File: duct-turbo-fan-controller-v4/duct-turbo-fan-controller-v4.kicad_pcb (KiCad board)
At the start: 2 copper layers, 42.7 x 48.8 mm, 45 parts, among them J1 Screw_Terminal_01x04, J2 Conn_01x04, J3 USB_OTG, J4 AudioJack4, J7 Conn_01x04, Q1 MMBT3904, Q2 BSS84, SW1 SW_Push, SW2 SW_Push, U1 SCD41-D-R2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

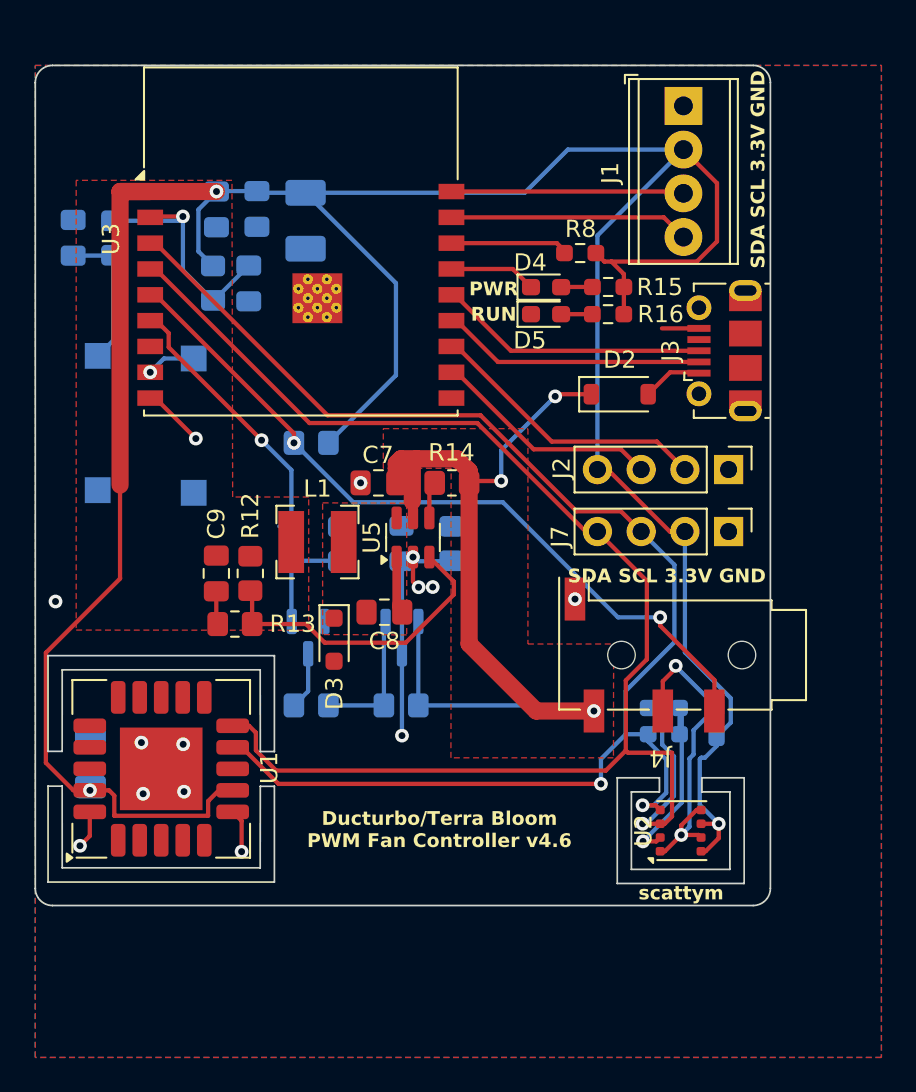
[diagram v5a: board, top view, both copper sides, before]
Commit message: Fix a couple of schematic errors.
1. External PWM was tied to ground.
2. BME688 SCA and SCL pins were tied together.
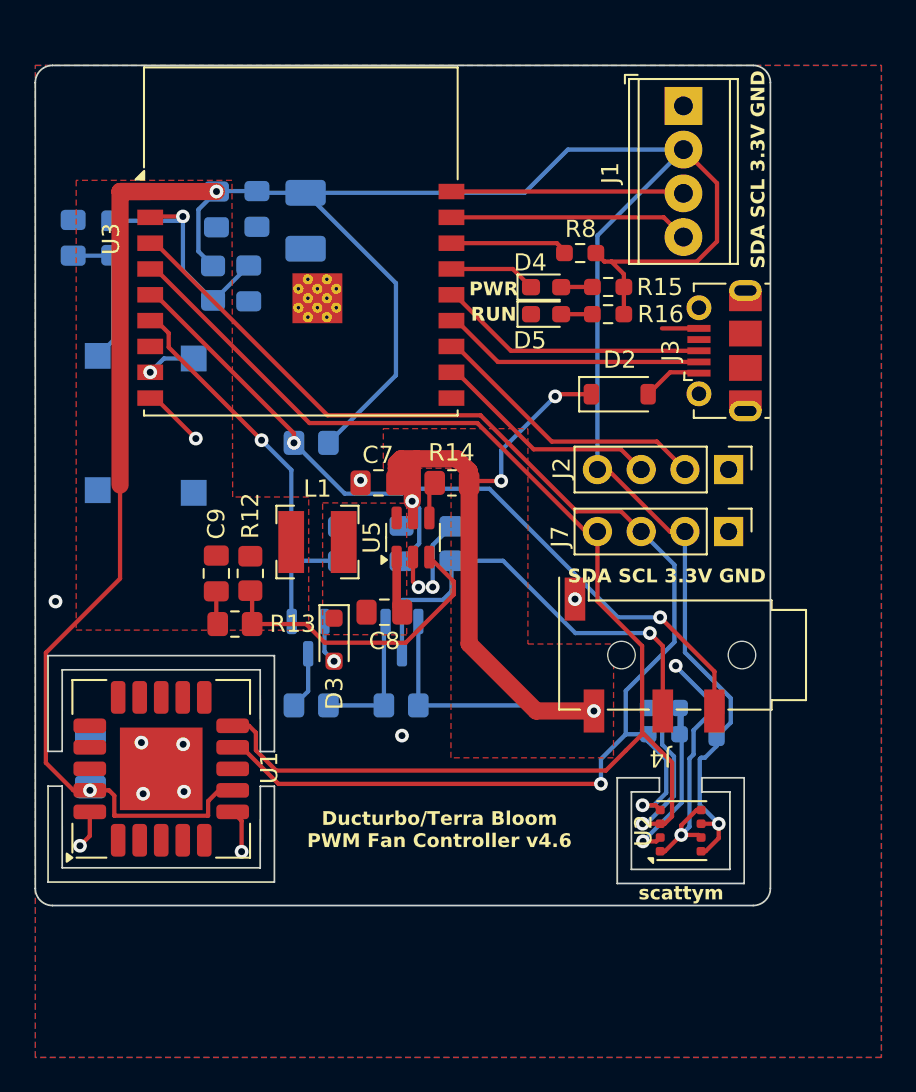
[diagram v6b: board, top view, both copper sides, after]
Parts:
- D1: value D_Zener_Small -> 12V Zener
- D4: value LED_Small -> LED Green
- D5: value LED_Small -> LED Red
- R15, R16: value R_Small -> 1k
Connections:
- D1 pad 1: GND -> +10V
- J4 pad R1: GND -> Net-(Q2-D)
- Q2 pad 3: GND -> Net-(Q2-D)
- R5 pad 1: GND -> Net-(Q2-D)
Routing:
- net Net-(Q2-D): track 0.00 -> 26.1 mm, vias 0 -> 1
- net GND: track 54.6 -> 37.1 mm
- net +10V: track 53.8 -> 57.7 mm, vias 3 -> 4
- net +3V3: track 179.9 -> 177.2 mm
- net BME688_SDA: track 88.3 -> 86.2 mm
- net BME688_SCL: track 83.4 -> 82.1 mm
- net GPIO_PWM: track 16.3 -> 15.2 mm

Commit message: Bump board version.
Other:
- board text added: "Ducturbo/Terra Bloom PWM Fan Controller v4.7"
- board text removed: "Ducturbo/Terra Bloom PWM Fan Controller v4.6"
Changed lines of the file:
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@@
 		)
 	)
-	(gr_text "Ducturbo/Terra Bloom\nPWM Fan Controller v4.6"
+	(gr_text "Ducturbo/Terra Bloom\nPWM Fan Controller v4.7"
 		(at 96.5 91.5 0)
 		(layer "F.SilkS")
